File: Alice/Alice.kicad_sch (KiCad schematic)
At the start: 0 parts

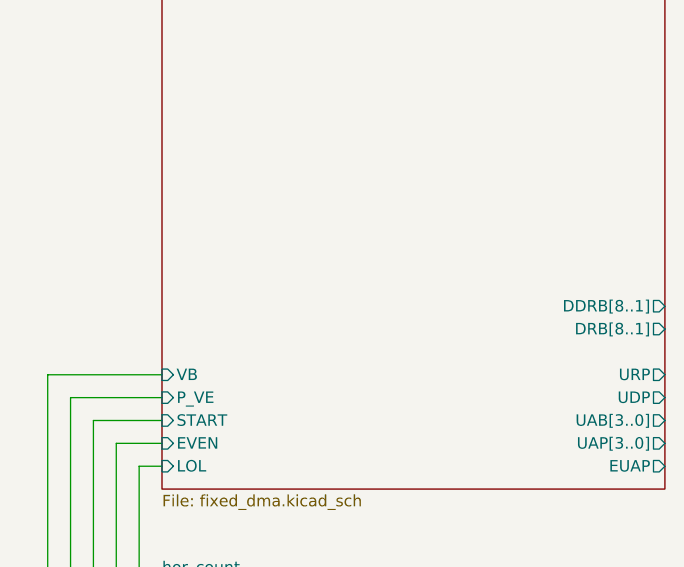
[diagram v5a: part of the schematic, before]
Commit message: RGA bus added (WIP), I/Os renamed with PAD_ prefix
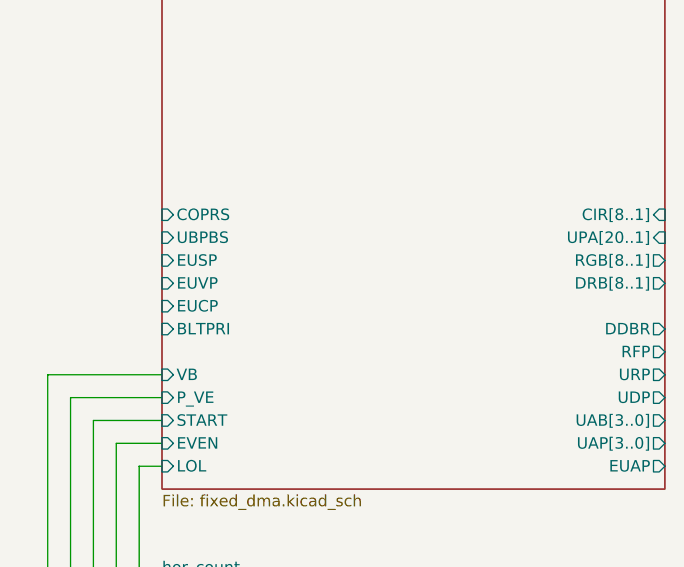
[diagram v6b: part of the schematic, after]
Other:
- sheet fixed_dma ports: added BLTPRI, CIR[8..1], COPRS, DDBR, EUCP, EUSP, EUVP, RFP, RGB[8..1], UBPBS, UPA[20..1]; removed DDRB[8..1]
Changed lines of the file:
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@@
       (effects (font (size 1.27 1.27)) (justify right))
     )
-    (pin "DRB[8..1]" output (at 434.34 264.16 0)
+    (pin "DRB[8..1]" output (at 434.34 259.08 0)
       (effects (font (size 1.27 1.27)) (justify right))
     )
@@
       (effects (font (size 1.27 1.27)) (justify right))
     )
-    (pin "DDRB[8..1]" output (at 434.34 261.62 0)
+    (pin "UBPBS" input (at 378.46 254 180)
+      (effects (font (size 1.27 1.27)) (justify left))
+    )
+    (pin "EUSP" input (at 378.46 256.54 180)
+      (effects (font (size 1.27 1.27)) (justify left))
+    )
+    (pin "EUVP" input (at 378.46 259.08 180)
+      (effects (font (size 1.27 1.27)) (justify left))
+    )
+    (pin "EUCP" input (at 378.46 261.62 180)
+      (effects (font (size 1.27 1.27)) (justify left))
+    )
+    (pin "BLTPRI" input (at 378.46 264.16 180)
+      (effects (font (size 1.27 1.27)) (justify left))
+    )
+    (pin "DDBR" output (at 434.34 264.16 0)
+      (effects (font (size 1.27 1.27)) (justify right))
+    )
+    (pin "RGB[8..1]" output (at 434.34 256.54 0)
+      (effects (font (size 1.27 1.27)) (justify right))
+    )
+    (pin "COPRS" input (at 378.46 251.46 180)
+      (effects (font (size 1.27 1.27)) (justify left))
+    )
+    (pin "RFP" output (at 434.34 266.7 0)
+      (effects (font (size 1.27 1.27)) (justify right))
+    )
+    (pin "UPA[20..1]" input (at 434.34 254 0)
+      (effects (font (size 1.27 1.27)) (justify right))
+    )
+    (pin "CIR[8..1]" input (at 434.34 251.46 0)
       (effects (font (size 1.27 1.27)) (justify right))
     )
@@
       (reference "AND_42") (unit 1) (value "AND2") (footprint "")
     )
-    (path "/e894cc74-6f5d-406a-b8a9-c5dbe3f8ad47/fed98590-a6e1-4774-9ac5-6dd42197f19e"
+    (path "/e894cc74-6f5d-406a-b8a9-c5dbe3f8ad47/df9e479e-e9b8-46c3-b046-98d04ba7c1e4"
       (reference "AND_43") (unit 1) (value "AND3") (footprint "")
     )
@@
       (reference "AND_46") (unit 1) (value "AND2") (footprint "")
     )
+    (path "/e894cc74-6f5d-406a-b8a9-c5dbe3f8ad47/ce0204bb-4d02-4158-872f-13406cdbd744"
+      (reference "AND_47") (unit 1) (value "AND3") (footprint "")
+    )
+    (path "/e894cc74-6f5d-406a-b8a9-c5dbe3f8ad47/e603f5fd-8c2e-4e21-a337-ef185b04ba33"
+      (reference "AND_48") (unit 1) (value "AND3") (footprint "")
+    )
     (path "/d34432c0-ab02-4dab-851f-3fb8163b7223/c6da32e9-082f-42b3-8220-701866caef85"
       (reference "BEAMCON0_LB0") (unit 1) (value "LB2") (footprint "")
@@
       (reference "CSY_SR1") (unit 1) (value "SR") (footprint "")
     )
-    (path "/e894cc74-6f5d-406a-b8a9-c5dbe3f8ad47/2794c9aa-1127-4db2-9b3e-35f0e417d54a"
+    (path "/e894cc74-6f5d-406a-b8a9-c5dbe3f8ad47/d9ae218f-b604-4d6d-be0a-a86e9947a54a"
       (reference "DBR_FF1") (unit 1) (value "DFF") (footprint "")
+    )
+    (path "/e894cc74-6f5d-406a-b8a9-c5dbe3f8ad47/6be26fde-816a-4b04-8161-206faf15623e"
+      (reference "DBR_Q1") (unit 1) (value "PASS") (footprint "")
     )
     (path "/e894cc74-6f5d-406a-b8a9-c5dbe3f8ad47/13440c5c-2ff3-4b12-aa4a-e2cdfc74287b"
@@
       (reference "NOT_18") (unit 1) (value "NOT") (footprint "")
     )
+    (path "/e894cc74-6f5d-406a-b8a9-c5dbe3f8ad47/19841aaa-3aa3-4f85-b643-d3da99db2e3a"
+      (reference "NOT_19") (unit 1) (value "NOT") (footprint "")
+    )
+    (path "/e894cc74-6f5d-406a-b8a9-c5dbe3f8ad47/51f9cf42-53ef-4f0f-9eca-a8808182d099"
+      (reference "NOT_20") (unit 1) (value "NOT") (footprint "")
+    )
+    (path "/e894cc74-6f5d-406a-b8a9-c5dbe3f8ad47/1e12fc1d-20f7-4e62-a565-f6e7f4631dd0"
+      (reference "NOT_21") (unit 1) (value "NOT") (footprint "")
+    )
     (path "/2741f2f7-0689-47b7-9f91-a147d422d2dd/466ddeb0-f60d-4004-b8f0-c3c6cf3ba62f"
       (reference "OLDVB_SR1") (unit 1) (value "SR") (footprint "")
@@
       (reference "RFP_FF1") (unit 1) (value "DFF") (footprint "")
     )
+    (path "/e894cc74-6f5d-406a-b8a9-c5dbe3f8ad47/39427acb-960f-4550-ba6b-61d3e5cd6184"
+      (reference "RGA_INB1") (unit 1) (value "FAINB") (footprint "")
+    )
+    (path "/e894cc74-6f5d-406a-b8a9-c5dbe3f8ad47/0c57575e-c76c-4ce1-be77-d1e0a329fa18"
+      (reference "RGA_INB2") (unit 1) (value "FAINB") (footprint "")
+    )
+    (path "/e894cc74-6f5d-406a-b8a9-c5dbe3f8ad47/7d7ece72-2c08-44f0-83a9-d2df65bd6c0d"
+      (reference "RGA_INB3") (unit 1) (value "FAINB") (footprint "")
+    )
+    (path "/e894cc74-6f5d-406a-b8a9-c5dbe3f8ad47/22dedd4a-cbc8-4e21-a568-800399dd7682"
+      (reference "RGA_INB4") (unit 1) (value "FAINB") (footprint "")
+    )
+    (path "/e894cc74-6f5d-406a-b8a9-c5dbe3f8ad47/aa63b0bd-d670-4bd9-85cd-3a2777cb2a42"
+      (reference "RGA_INB5") (unit 1) (value "FAINB") (footprint "")
+    )
+    (path "/e894cc74-6f5d-406a-b8a9-c5dbe3f8ad47/f97af25d-99ad-41b5-96e5-c2f1b92dc779"
+      (reference "RGA_INB6") (unit 1) (value "FAINB") (footprint "")
+    )
+    (path "/e894cc74-6f5d-406a-b8a9-c5dbe3f8ad47/a4f4e71f-c853-4b7e-bee1-e2373b6b32a9"
+      (reference "RGA_INB7") (unit 1) (value "FAINB") (footprint "")
+    )
+    (path "/e894cc74-6f5d-406a-b8a9-c5dbe3f8ad47/54235019-2e42-4596-8877-80c587a06f86"
+      (reference "RGA_INB8") (unit 1) (value "FAINB") (footprint "")
+    )
+    (path "/e894cc74-6f5d-406a-b8a9-c5dbe3f8ad47/02fb4a95-a40d-4ffb-8f8e-c29a8ce1e663"
+      (reference "RGA_MUX1") (unit 1) (value "FAMUX") (footprint "")
+    )
+    (path "/e894cc74-6f5d-406a-b8a9-c5dbe3f8ad47/c3edeb58-90b9-41d0-8072-f6ae61b29dbc"
+      (reference "RGA_MUX2") (unit 1) (value "FAMUX") (footprint "")
+    )
+    (path "/e894cc74-6f5d-406a-b8a9-c5dbe3f8ad47/f6dd32b3-83d8-49a3-958a-779458118d6b"
+      (reference "RGA_MUX3") (unit 1) (value "FAMUX") (footprint "")
+    )
+    (path "/e894cc74-6f5d-406a-b8a9-c5dbe3f8ad47/167be6af-0848-48b3-ad75-d28829a4017f"
+      (reference "RGA_MUX4") (unit 1) (value "FAMUX") (footprint "")
+    )
+    (path "/e894cc74-6f5d-406a-b8a9-c5dbe3f8ad47/fc177e1a-b8ac-4aaa-ad9d-002772094d93"
+      (reference "RGA_MUX5") (unit 1) (value "FAMUX") (footprint "")
+    )
+    (path "/e894cc74-6f5d-406a-b8a9-c5dbe3f8ad47/91f5d199-e220-40ec-805d-52774f308f77"
+      (reference "RGA_MUX6") (unit 1) (value "FAMUX") (footprint "")
+    )
+    (path "/e894cc74-6f5d-406a-b8a9-c5dbe3f8ad47/456ed35e-ace7-41d5-a2ae-25c68a4c2991"
+      (reference "RGA_MUX7") (unit 1) (value "FAMUX") (footprint "")
+    )
+    (path "/e894cc74-6f5d-406a-b8a9-c5dbe3f8ad47/eff76857-d39a-48c8-9503-2395161e61de"
+      (reference "RGA_MUX8") (unit 1) (value "FAMUX") (footprint "")
+    )
     (path "/e894cc74-6f5d-406a-b8a9-c5dbe3f8ad47/d48cfc93-78b1-4b3a-9e54-6f76ae4f863d"

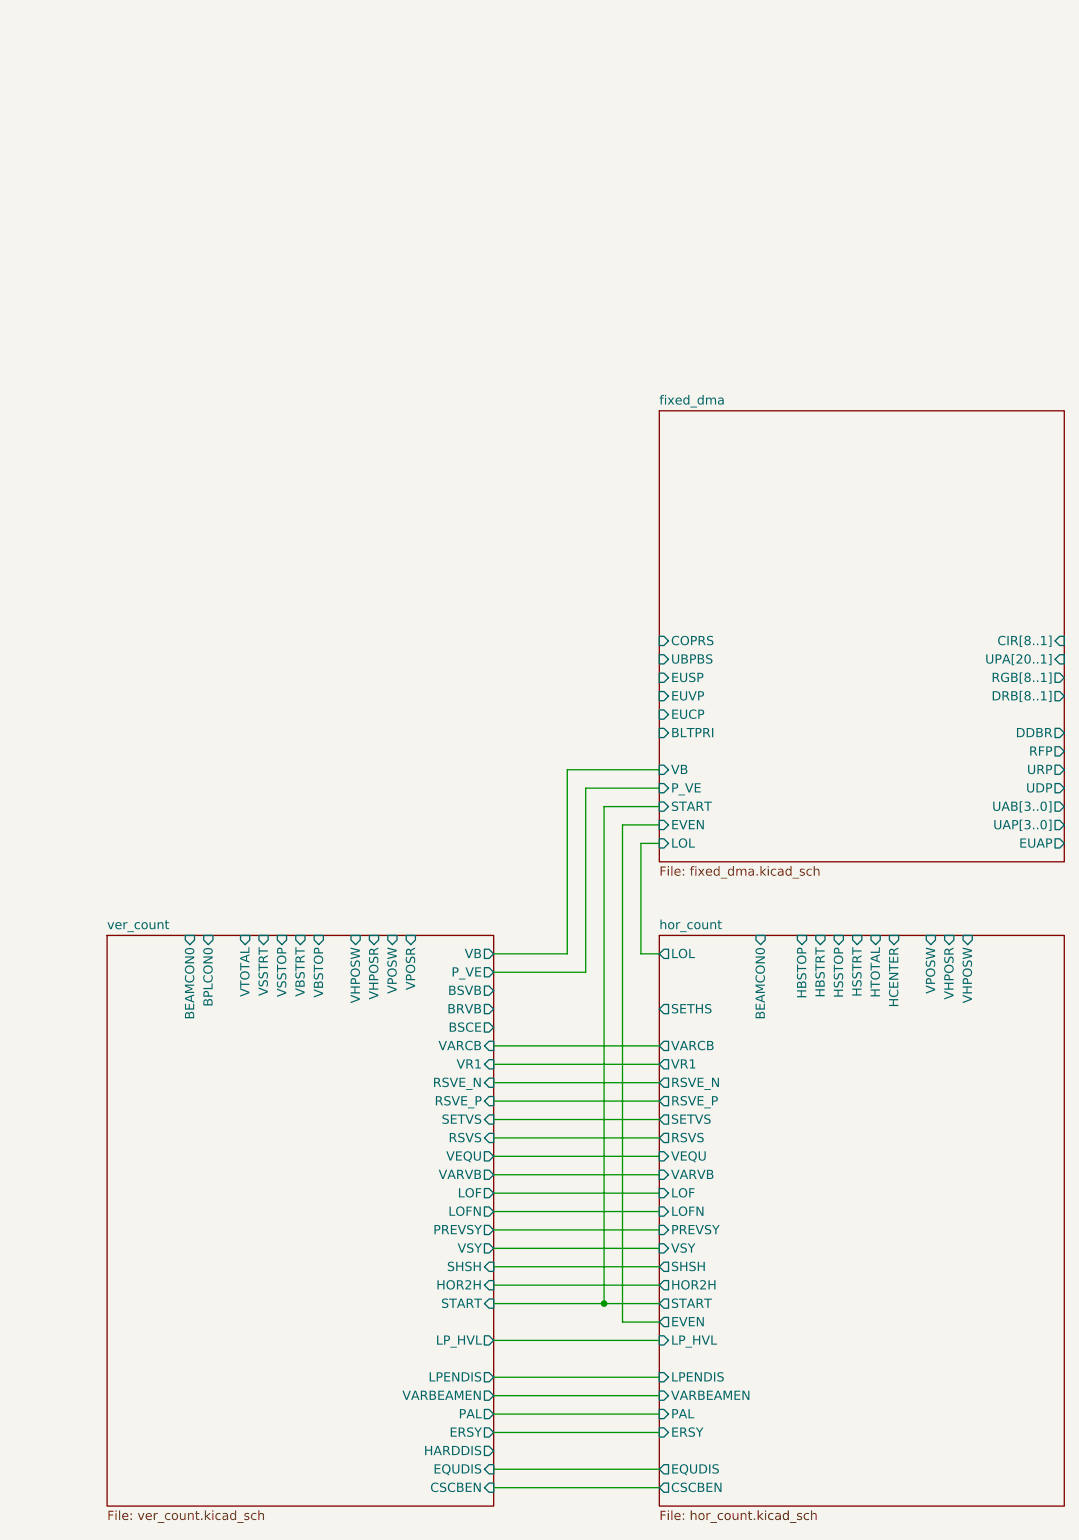
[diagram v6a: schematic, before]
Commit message: Sheet RGA decode added
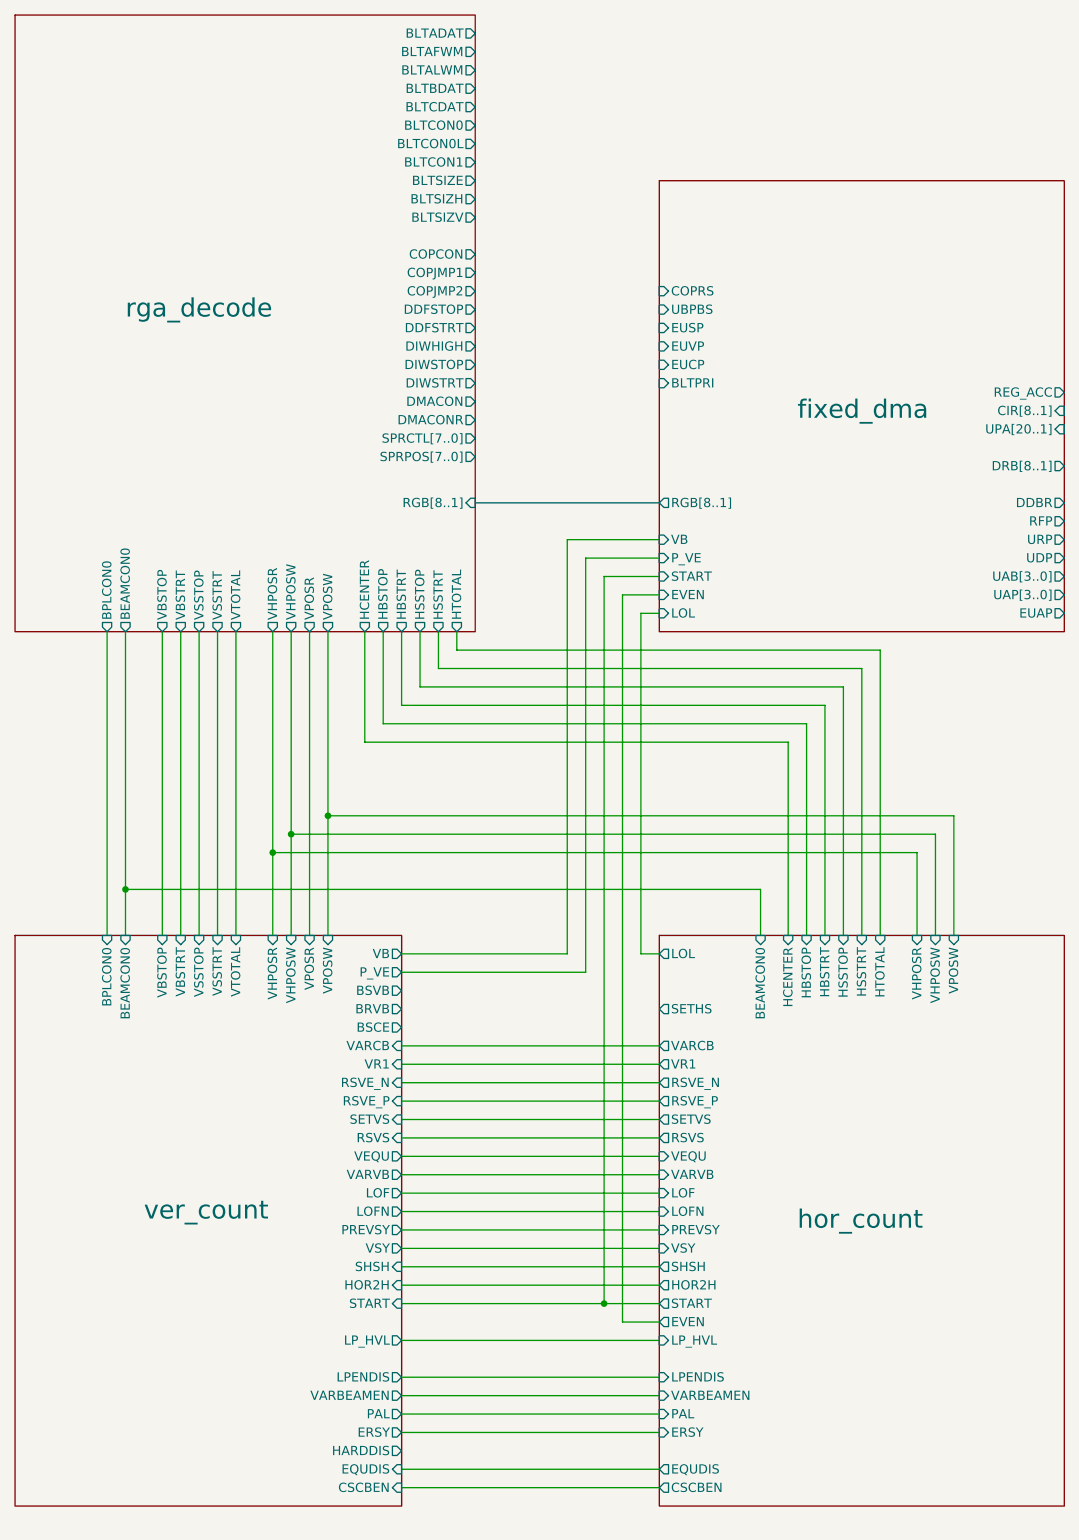
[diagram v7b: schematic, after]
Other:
- added sheet rga_decode (rga_decode.kicad_sch)
- sheet fixed_dma ports: added REG_ACC; removed none
